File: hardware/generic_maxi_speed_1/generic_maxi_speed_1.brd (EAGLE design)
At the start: 50 x 50 mm, 31 parts, among them IC1 MEGA48/88/168-PU, IC2 RFM12, IC3 LP2950Z, Q1 20MHz

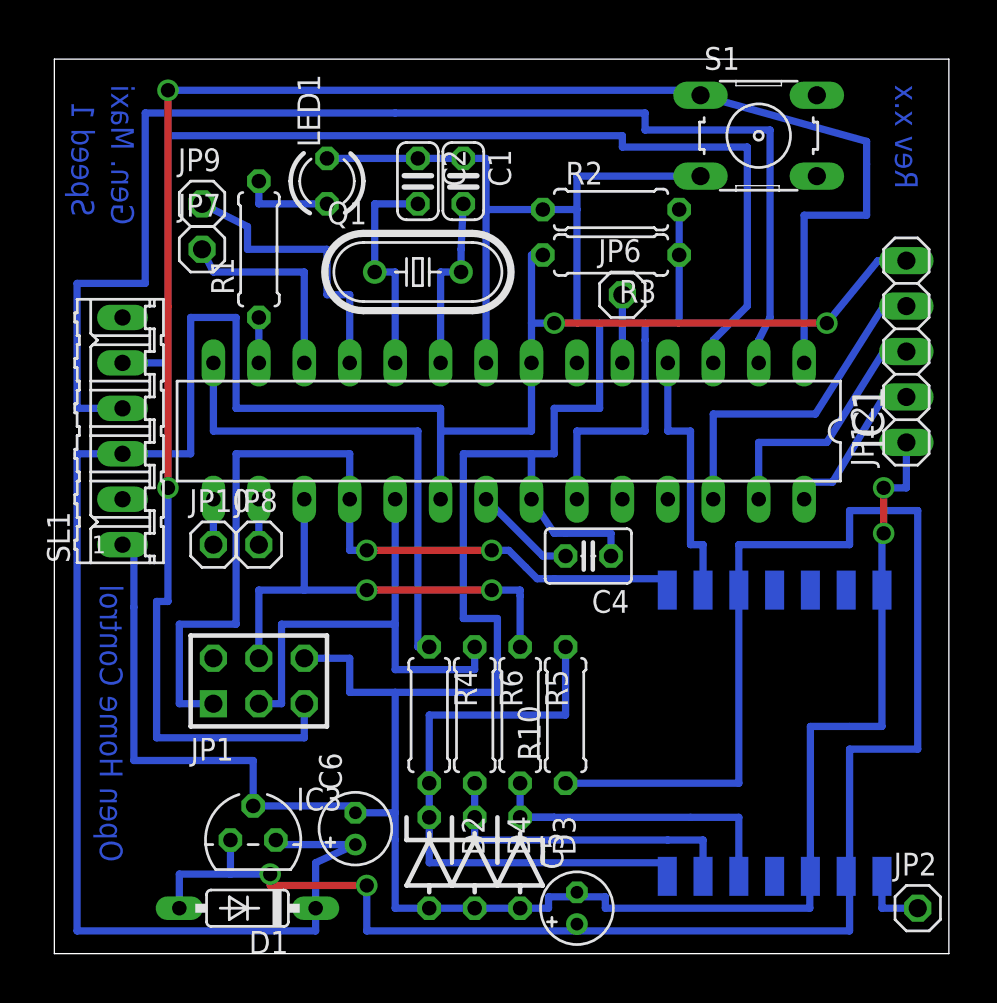
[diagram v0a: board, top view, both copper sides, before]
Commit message: Improved distance between some pcb tracks.
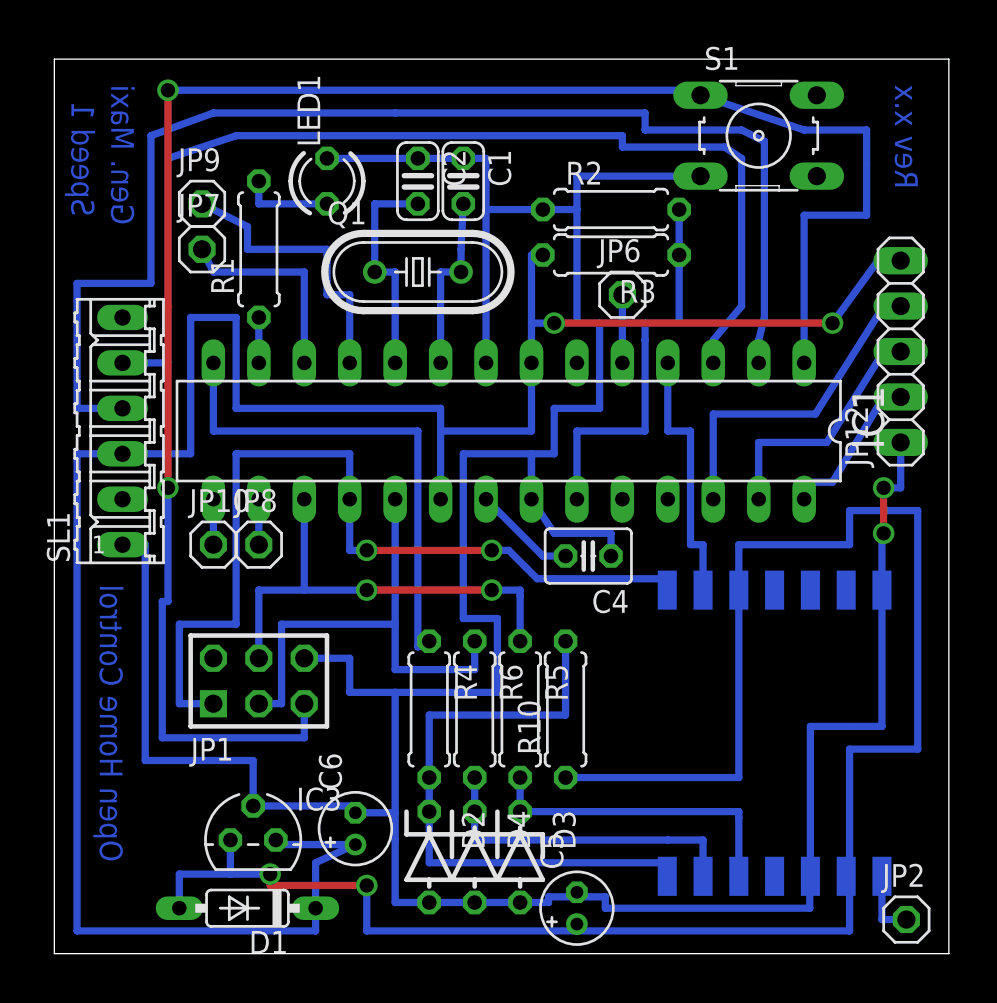
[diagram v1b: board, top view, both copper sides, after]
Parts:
- moved JP2 0.90 mm to (47.6, 1.91)
- moved JP12 0.32 mm to (47.3, 33.7)
- moved D2 0.32 mm to (21.0, 5.40)
- moved D3 0.32 mm to (26.0, 5.40)
- moved D4 0.32 mm to (23.5, 5.40)
- moved R10 0.32 mm to (28.6, 13.7)
- moved R4 0.32 mm to (21.0, 13.7)
- moved R5 0.32 mm to (26.0, 13.7)
- moved R6 0.32 mm to (23.5, 13.7)
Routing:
- net N$9: track 61.1 -> 59.1 mm
- net N$10: track 71.9 -> 69.9 mm
- net N$16: track 19.3 -> 17.7 mm
- net GND: track 194.9 -> 193.9 mm

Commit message: Rev 1.0 finished, circuit working. Add mask and placing picture.
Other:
- board text added: "H:/Eigene Dateien/ohc/logo/logo_black 150x133.bmp"
- board text added: "Rev 1.0"
- board text removed: "Rev x.x"

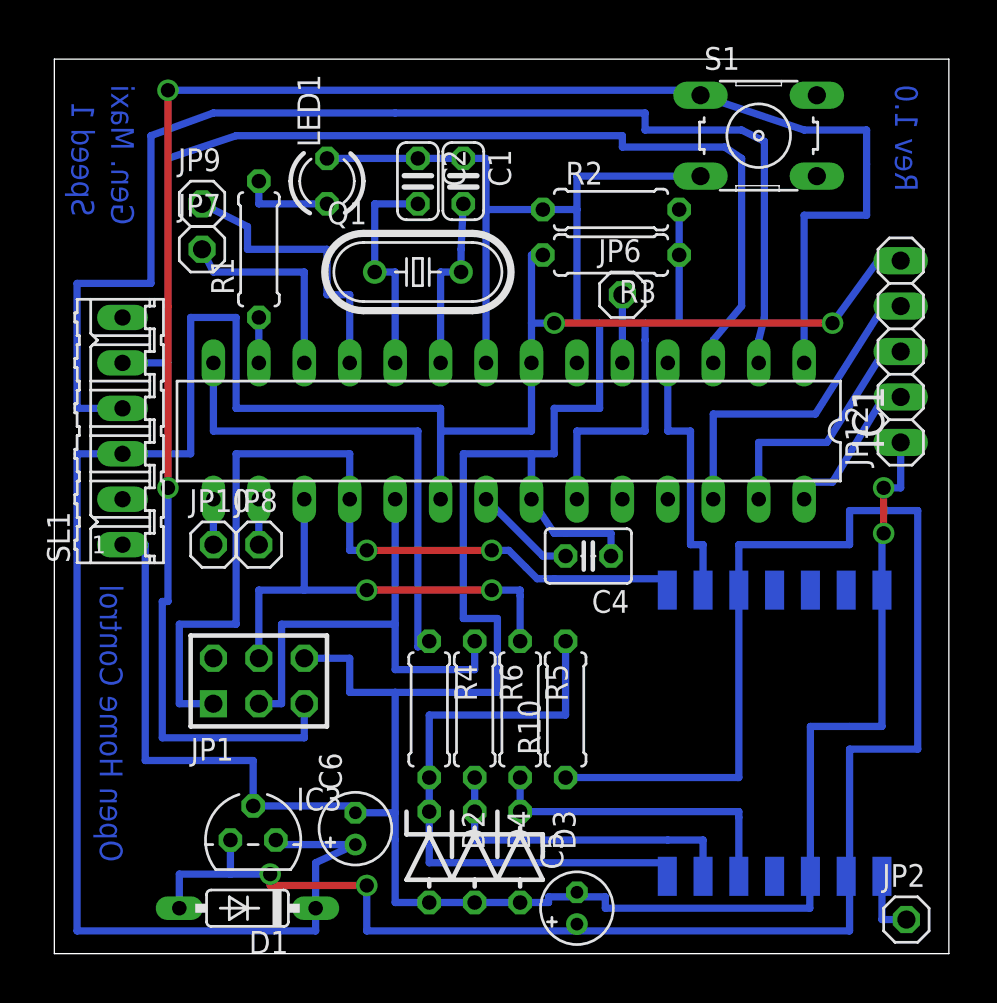
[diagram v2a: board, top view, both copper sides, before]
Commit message: optimized label positions. Rename ATMega model in label.
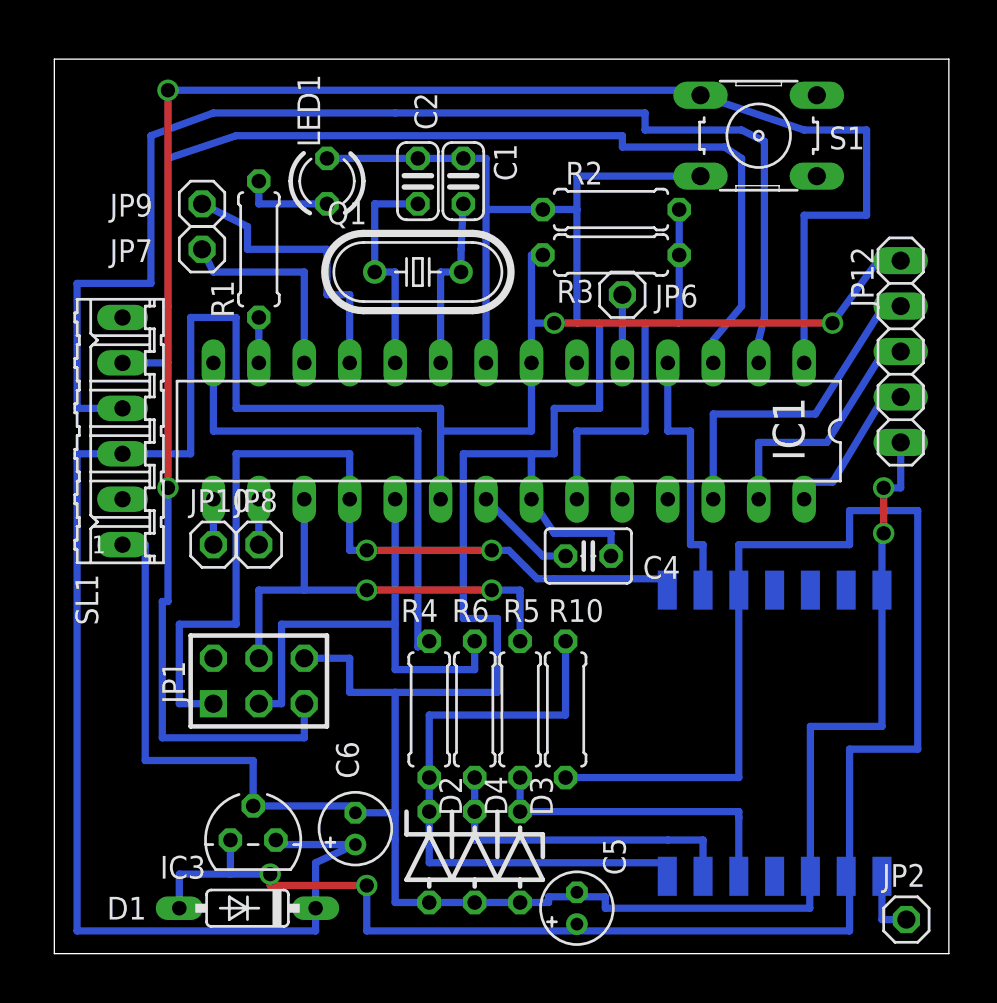
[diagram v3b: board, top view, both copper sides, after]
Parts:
- IC1: value MEGA48/88/168-PU -> MEGA168/328
- JP10, JP6, JP7, JP8, JP9: value ANT -> (none)
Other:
- board text added: "D:/Eigene Dateien/ohc/logo/logo_black 150x133.bmp"
